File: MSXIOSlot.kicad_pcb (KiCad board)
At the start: 2 copper layers, 83.1 x 74.4 mm, 14 parts, among them J1 Conn_02x25_Odd_Even, J2 Conn_02x25_Odd_Even, J3 Conn_02x25_Odd_Even, U1 74LS21

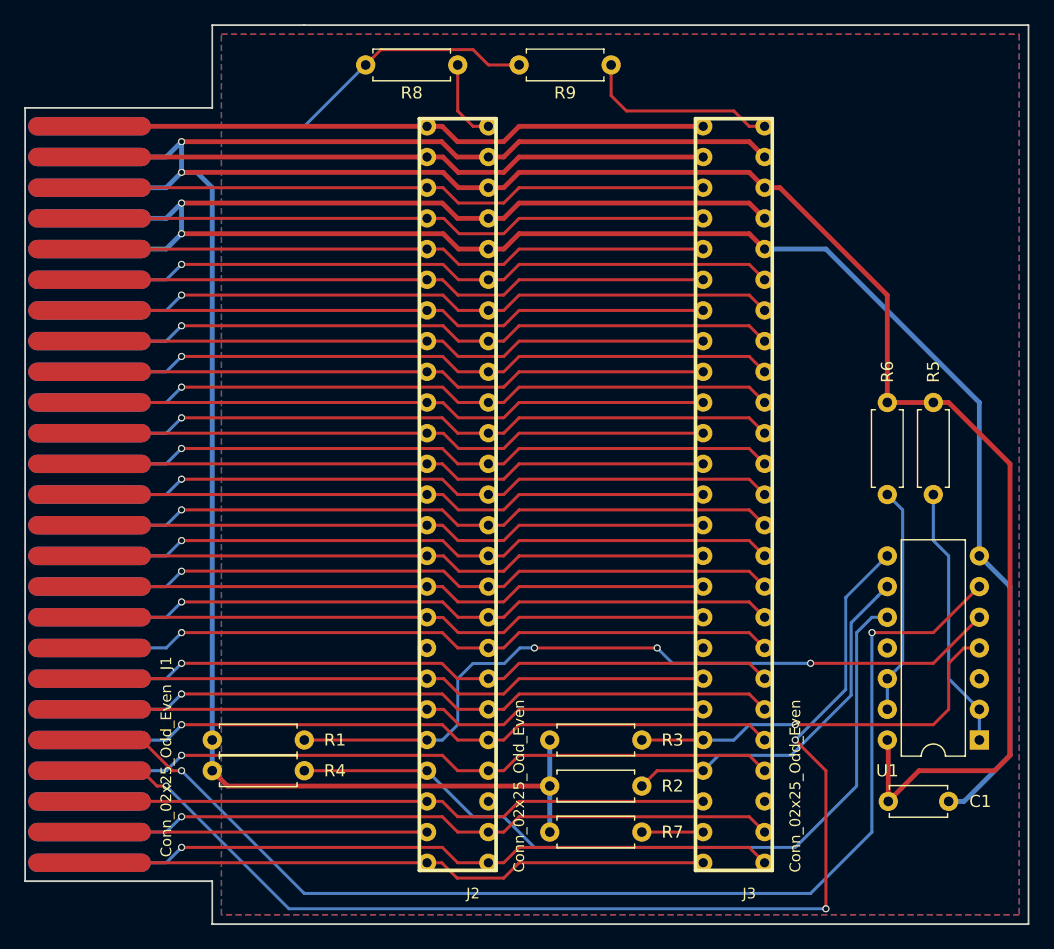
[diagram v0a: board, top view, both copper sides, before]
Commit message: move audio resisters for better connector clearance
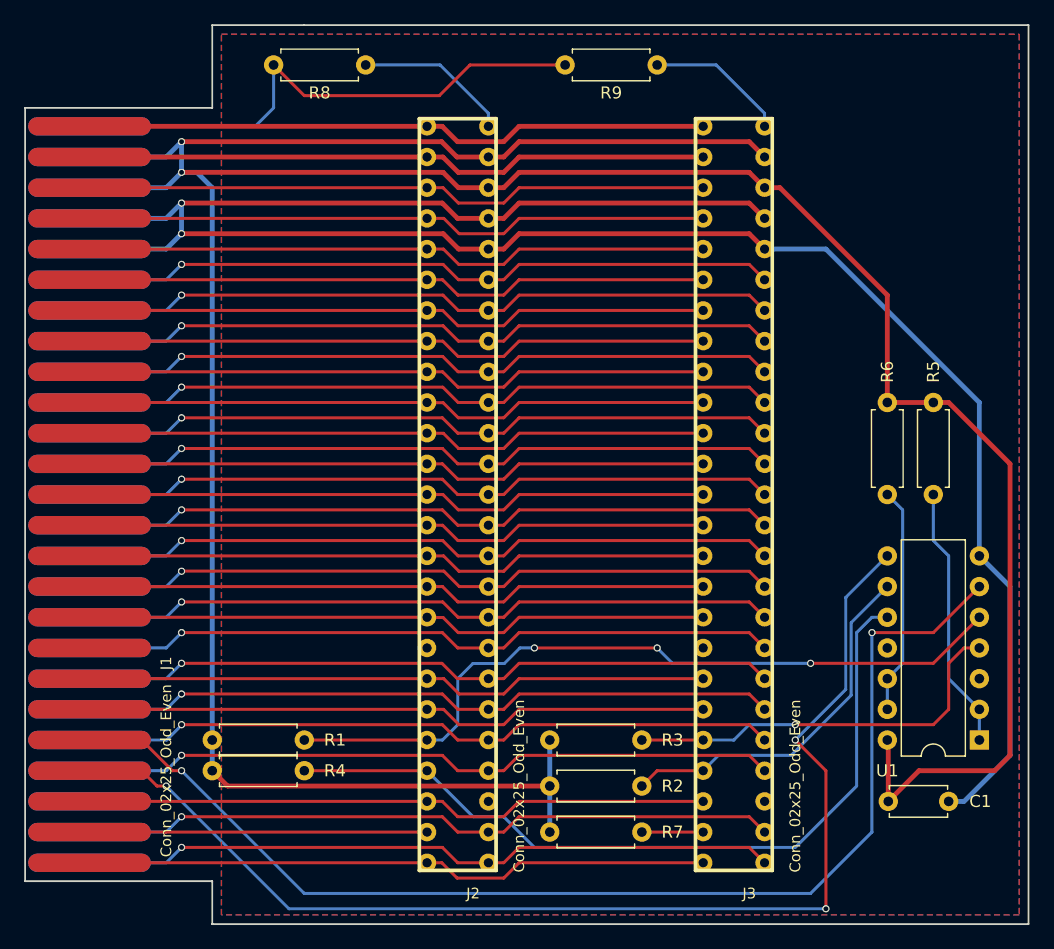
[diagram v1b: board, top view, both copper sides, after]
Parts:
- moved R8 7.62 mm to (109.2, 77.5)
- moved R9 3.81 mm to (133.3, 77.5)
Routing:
- net SOUNDIN: track 38.7 -> 45.7 mm
- net SOUND_A: track 6.88 -> 12.9 mm
- net /BUSDIR: track 104.2 -> 99.1 mm
- net SOUND_B: track 16.3 -> 11.6 mm
